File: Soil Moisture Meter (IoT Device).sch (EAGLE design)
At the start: 19 parts, among them J1 ICSP, Q1 32.768 kHz, U1 MSP430FR4133

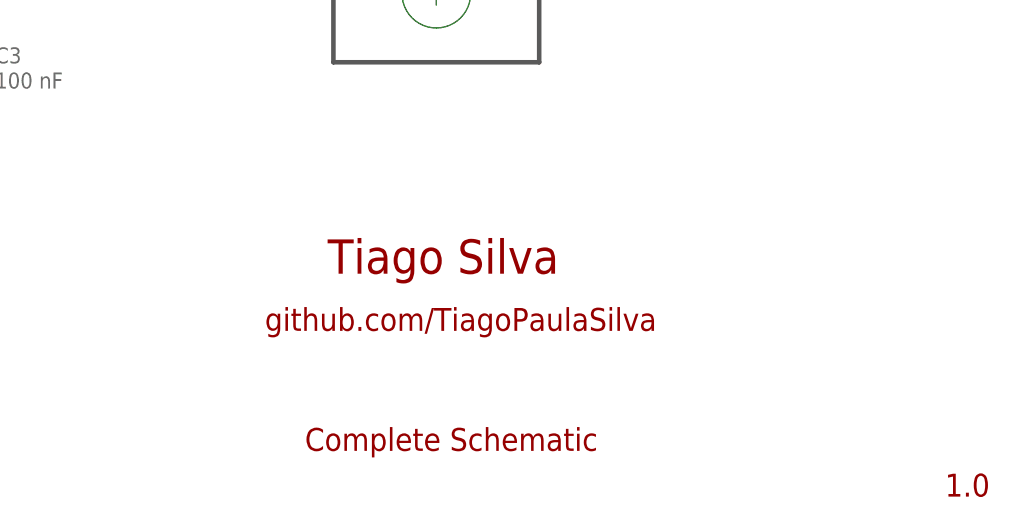
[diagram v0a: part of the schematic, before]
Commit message: Schematic frame info updated
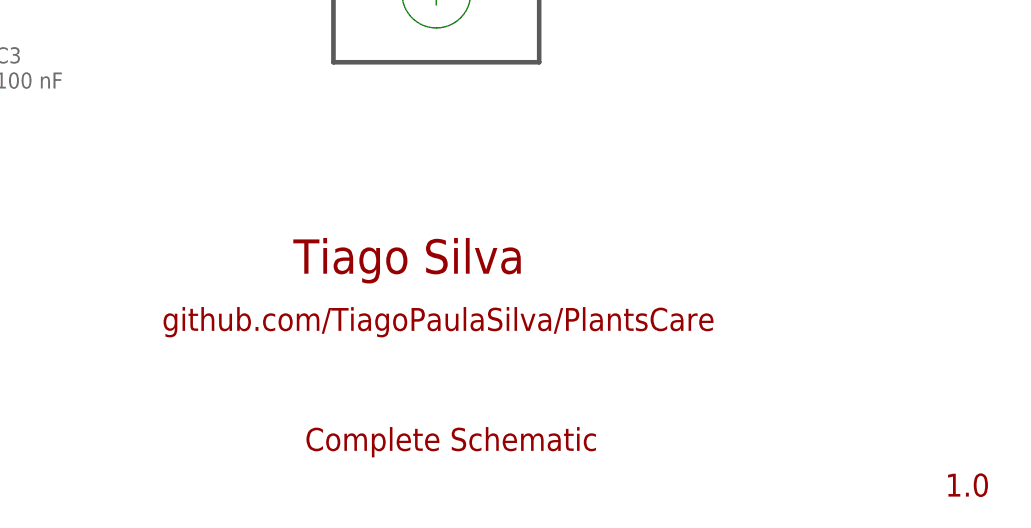
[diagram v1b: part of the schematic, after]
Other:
- note added: "github.com/TiagoPaulaSilva/PlantsCare"
- note removed: "github.com/TiagoPaulaSilva"
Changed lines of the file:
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@@
 <sheet>
 <plain>
-<text x="184.785" y="26.035" size="3.81" layer="94">Tiago Silva</text>
-<text x="177.8" y="19.685" size="2.54" layer="94">github.com/TiagoPaulaSilva</text>
+<text x="180.975" y="26.035" size="3.81" layer="94">Tiago Silva</text>
+<text x="166.37" y="19.685" size="2.54" layer="94">github.com/TiagoPaulaSilva/PlantsCare</text>
 <wire x1="185.42" y1="87.63" x2="185.42" y2="49.53" width="0.508" layer="97"/>
 <wire x1="185.42" y1="49.53" x2="208.28" y2="49.53" width="0.508" layer="97"/>
@@
 </sheet>
 </sheets>
+<errors>
+</errors>
 </schematic>
 </drawing>

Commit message: PCB layout developed
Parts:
- added BT1: CR2450, 1053:1053
- added R6, R7: 10k, rcl:R-EU_R0603
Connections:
- net SENSOR_OUTPUT renamed ELECTRODE_CAP2
- new net ELECTRODE_CAP1: R6.1, R7.2
- net 3V: now also BT1.3V
- net BUTTON_PROG: now also U1.P1.7/TA0.1/TDO/A7; no longer U1.P1.2/UCA0CLK/A2
- net GND: now also BT1.GND, R6.2, R7.1
- net HF_SQUAREWAVE: now also U1.P7.0/L0; no longer U1.P2.0/L24
- net SENSOR_VOUT: now also U1.P1.2/UCA0CLK/A2; no longer U1.P1.7/TA0.1/TDO/A7
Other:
- moved on the sheet: C1, C2, J1-1, J1-2, J1-3, J1-4
